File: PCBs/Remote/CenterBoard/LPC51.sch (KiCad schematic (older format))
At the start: 23 parts, among them J201 DX07S016JA1R1500, U201 LPC51U68JBD64

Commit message: Bezig met LEDS
Signed-off-by: Eldalote.Electronics <Eldalote.Electronics@gmail.com>
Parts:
- added C?: 100nF, Capacitor_SMD:C_0402_1005Metric, symbol Device:C_Small
- added U?: W25Q128JVS, Package_SO:SOIC-8_5.23x5.23mm_P1.27mm, symbol Memory_Flash:W25Q128JVS
- R201, R202: footprint Resistor_SMD:R_0805_2012Metric_Pad1.15x1.40mm_HandSolder -> Resistor_SMD:R_0603_1608Metric_Pad1.05x0.95mm_HandSolder; DigiKey P123897CT-ND -> P123790CT-ND; Mouser 667-ERA-6AHD330V -> 667-ERA-3AHD330V
- R203, R204, R205, R206: footprint Resistor_SMD:R_0805_2012Metric_Pad1.15x1.40mm_HandSolder -> Resistor_SMD:R_0603_1608Metric_Pad1.05x0.95mm_HandSolder; DigiKey P3.3KBNCT-ND -> P123763CT-ND; LCSC C26010 -> C22978; Mouser 667-ERA-6AED332V -> 667-ERA-3AED332V
- S201, S202: Category Switches -> (none); DK_Datasheet_Link https://www.te.com/commerce/DocumentDelivery/DDEController?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 -> (none); DK_Detail_Page /product-detail/en/te-connectivity-alcoswitch-switches/1825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 -> (none); Description SWITCH TACTILE SPST-NO 0.05A 24V -> (none); Digi-Key_PN 450-1650-ND -> (none); DigiKey (none) -> 450-1650-ND; Family Tactile Switches -> (none); MPN 1825910-6 -> (none); Manufacturer TE Connectivity ALCOSWITCH Switches -> (none); Mouser (none) -> 506-FSM4JH; Status Active -> (none)
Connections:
- net +3V3: now also C?.1, U?.8 (VCC)
- net GND: now also C?.2, U?.4 (GND)

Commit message: Continued work with the center board
Signed-off-by: Eldalote.Electronics <Eldalote.Electronics@gmail.com>
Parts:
- U201: DigiKey (none) -> 568-13909-ND; Mouser (none) -> 771-LPC51U68JBD64QL
- U202: renamed from U?; LCSC (none) -> C97521
- gave numbers to parts that had none: 1
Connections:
- net Flash_SPI_MISO: now reaches U202.2 (DO(IO1))
- net Flash_SPI_MOSI: now reaches U202.5 (DI(IO0))
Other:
- note added: "USB Connector"
- note added: "User Flash"
- moved on the sheet: C201, C202, C203, C204, C205, C206, C207, C208, C209, C210, C211, C212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

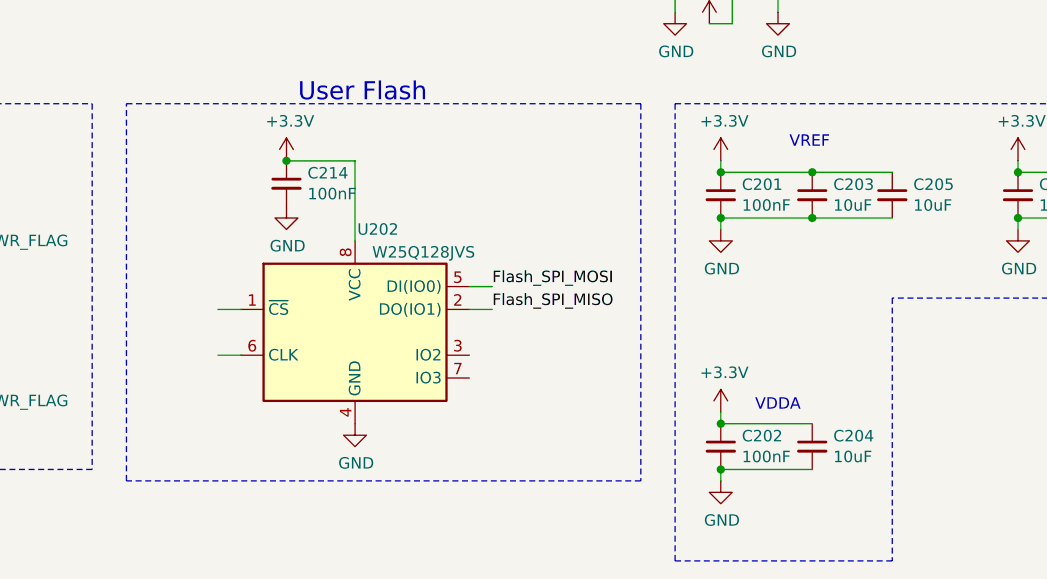
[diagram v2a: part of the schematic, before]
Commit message: Note: Schmitt trigger for joystick Buttons TODO
Signed-off-by: Eldalote.Electronics <Eldalote.Electronics@gmail.com>
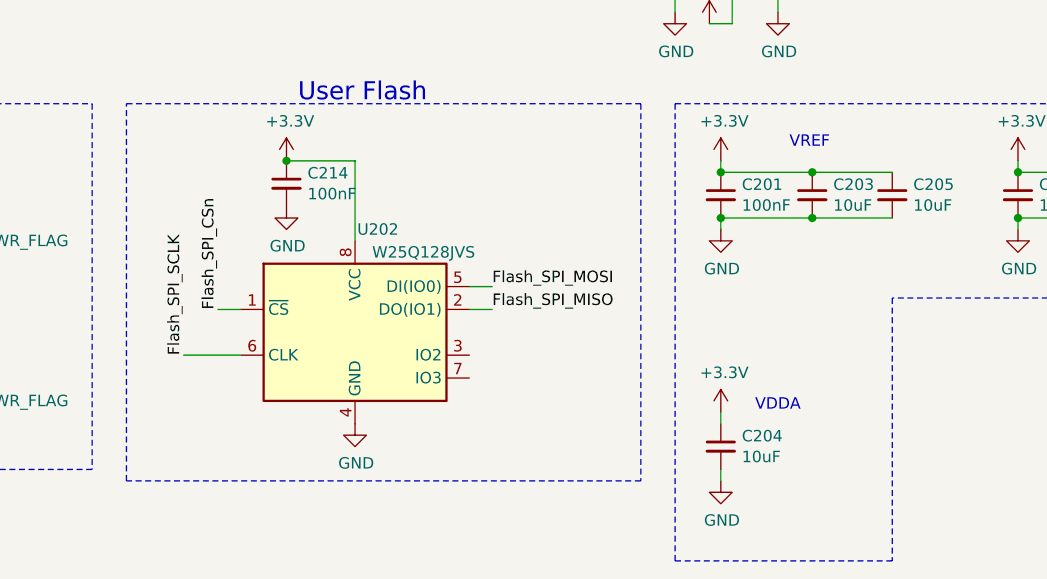
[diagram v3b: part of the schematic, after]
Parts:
- removed C202: 100nF, Capacitor_SMD:C_0805_2012Metric_Pad1.15x1.40mm_HandSolder, symbol Device:C_Small
- C201, C206, C208, C210, C212: footprint Capacitor_SMD:C_0805_2012Metric_Pad1.15x1.40mm_HandSolder -> Capacitor_SMD:C_0402_1005Metric; DigiKey 1276-1099-1-ND -> (none); LCSC C49678 -> C1525; Mouser 187-CL21B104KACNNNC -> (none)
- C203, C204, C205: footprint Capacitor_SMD:C_0805_2012Metric_Pad1.15x1.40mm_HandSolder -> Capacitor_SMD:C_0402_1005Metric; DigiKey 1276-2891-1-ND -> (none); LCSC C15850 -> C15525; Mouser 187-CL21A106KAYNNNE -> (none)
- C207, C209, C211, C213: footprint Capacitor_SMD:C_0805_2012Metric_Pad1.15x1.40mm_HandSolder -> Capacitor_SMD:C_0402_1005Metric; DigiKey 1276-1015-1-ND -> 1276-1028-1-ND; LCSC C1710 -> C15195; Mouser 187-CL21B103KBANNNC -> 187-CL05B103KB5NNNC
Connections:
- net Flash_SPI_CSn: now reaches U202.1 (~CS)
- net Flash_SPI_SCLK: now reaches U202.6 (CLK)

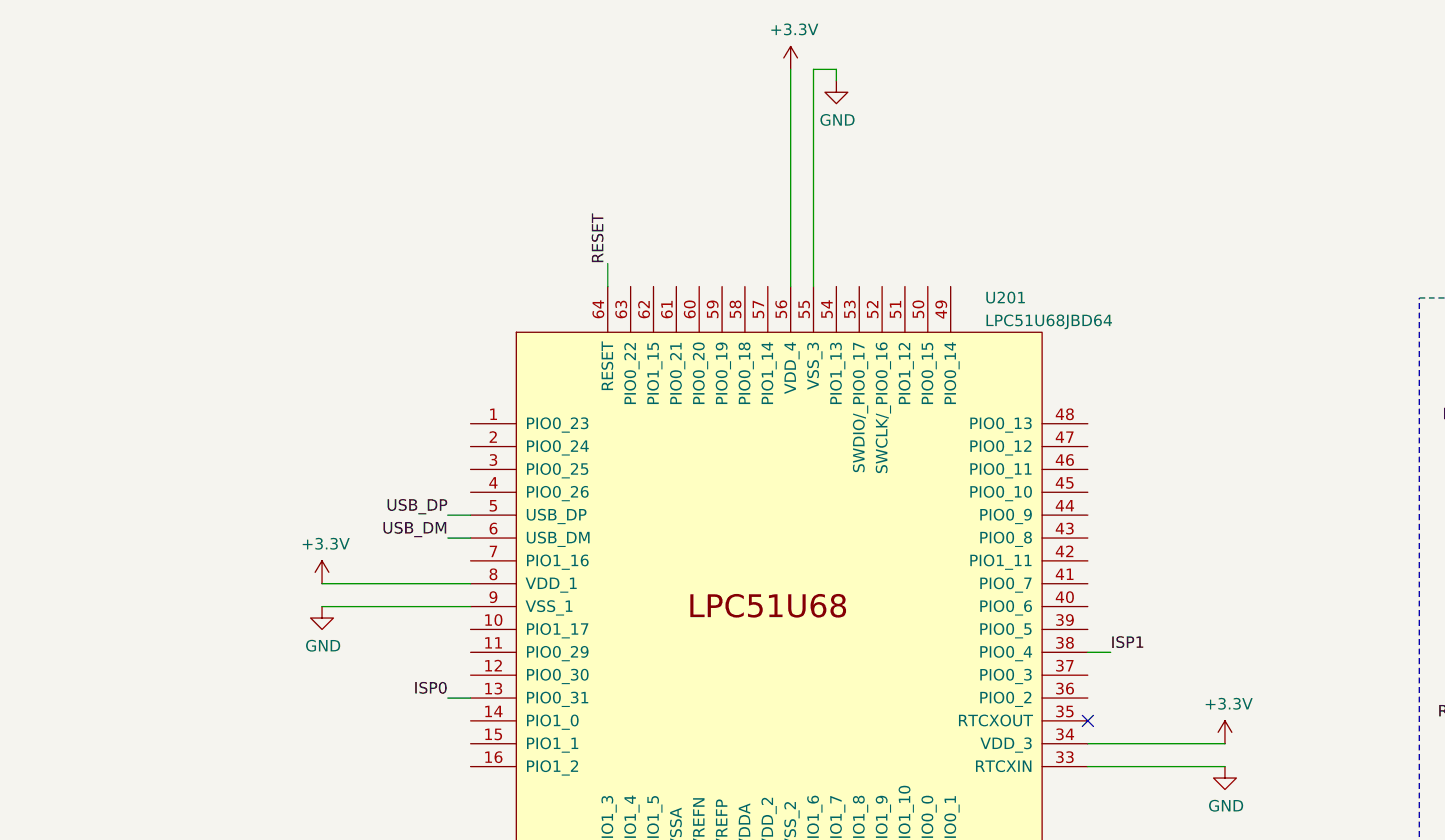
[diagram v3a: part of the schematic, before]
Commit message: Made the keyboard PCB. With LPC software started pin assignment on the LPC
Signed-off-by: Eldalote.Electronics <Eldalote.Electronics@gmail.com>
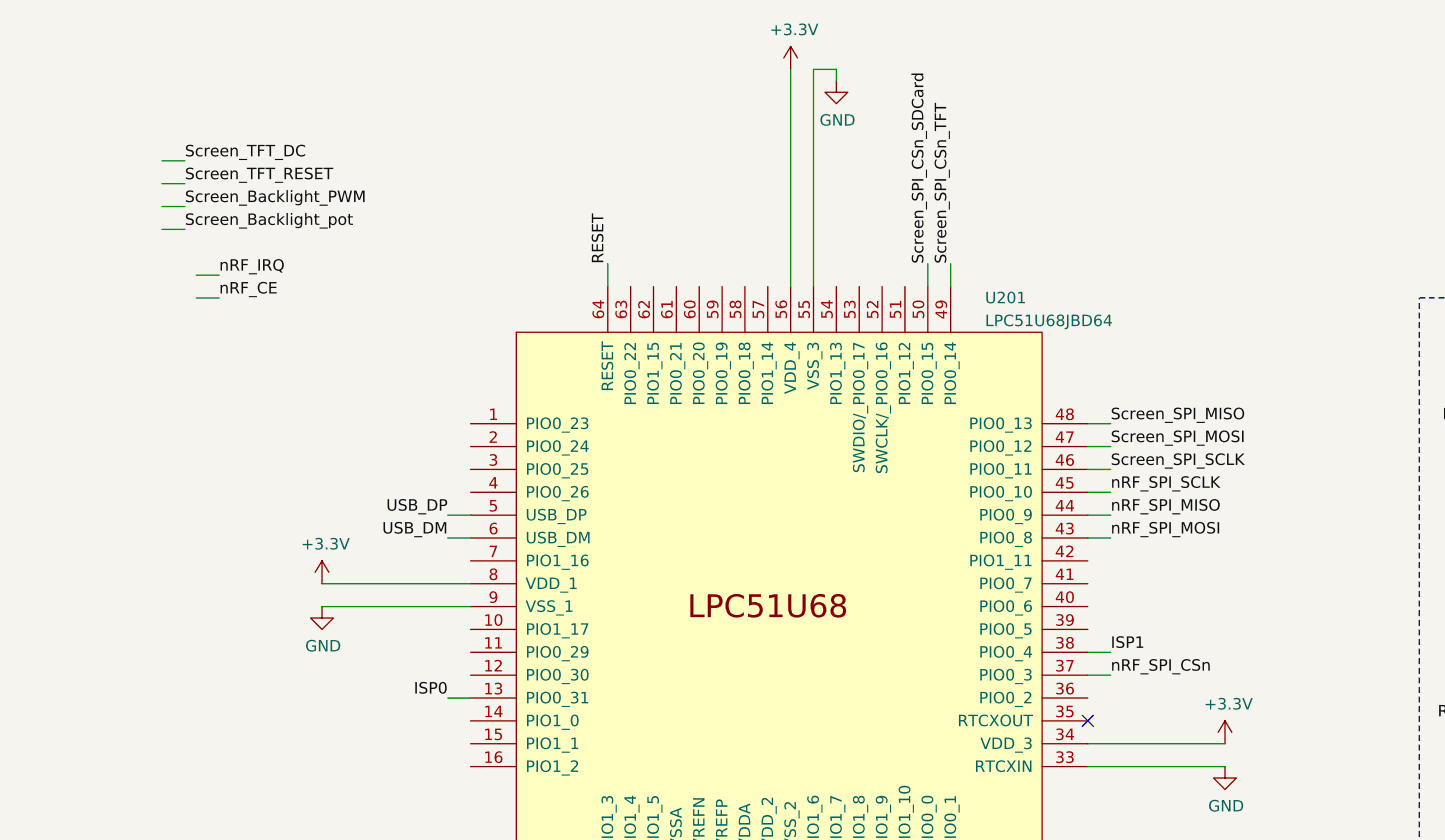
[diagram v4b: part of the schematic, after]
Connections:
- wire segments 117 -> 132
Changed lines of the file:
@@
 $Descr A4 11693 8268
 encoding utf-8
-Sheet 2 6
+Sheet 2 7
 Title ""
 Date ""
@@
 Text Label 3800 6650 1    50   ~ 0
 Flash_SPI_SCLK
+Wire Wire Line
+	7700 2800 7800 2800
+Wire Wire Line
+	7700 2700 7800 2700
+Wire Wire Line
+	7700 2600 7800 2600
+Wire Wire Line
+	7700 3400 7800 3400
+Wire Wire Line
+	3800 1750 3900 1750
+Wire Wire Line
+	3800 1650 3900 1650
+Text Label 7800 2600 0    50   ~ 0
+nRF_SPI_SCLK
+Text Label 7800 2700 0    50   ~ 0
+nRF_SPI_MISO
+Text Label 7800 2800 0    50   ~ 0
+nRF_SPI_MOSI
+Text Label 7800 3400 0    50   ~ 0
+nRF_SPI_CSn
+Text Label 3900 1650 0    50   ~ 0
+nRF_IRQ
+Text Label 3900 1750 0    50   ~ 0
+nRF_CE
+Wire Wire Line
+	3750 1450 3650 1450
+Text Label 3750 1450 0    50   ~ 0
+Screen_Backlight_pot
+Wire Wire Line
+	7700 2500 7800 2500
+Wire Wire Line
+	7700 2300 7800 2300
+Wire Wire Line
+	7700 2400 7800 2400
+Wire Wire Line
+	7100 1700 7100 1600
+Wire Wire Line
+	3650 1250 3750 1250
+Wire Wire Line
+	3650 1150 3750 1150
+Wire Wire Line
+	7000 1700 7000 1600
+Wire Wire Line
+	3650 1350 3750 1350
+Text Label 7800 2500 0    50   ~ 0
+Screen_SPI_SCLK
+Text Label 7800 2300 0    50   ~ 0
+Screen_SPI_MISO
+Text Label 7800 2400 0    50   ~ 0
+Screen_SPI_MOSI
+Text Label 7100 1600 1    50   ~ 0
+Screen_SPI_CSn_TFT
+Text Label 3750 1250 0    50   ~ 0
+Screen_TFT_RESET
+Text Label 3750 1150 0    50   ~ 0
+Screen_TFT_DC
+Text Label 7000 1600 1    50   ~ 0
+Screen_SPI_CSn_SDCard
+Text Label 3750 1350 0    50   ~ 0
+Screen_Backlight_PWM
 $EndSCHEMATC

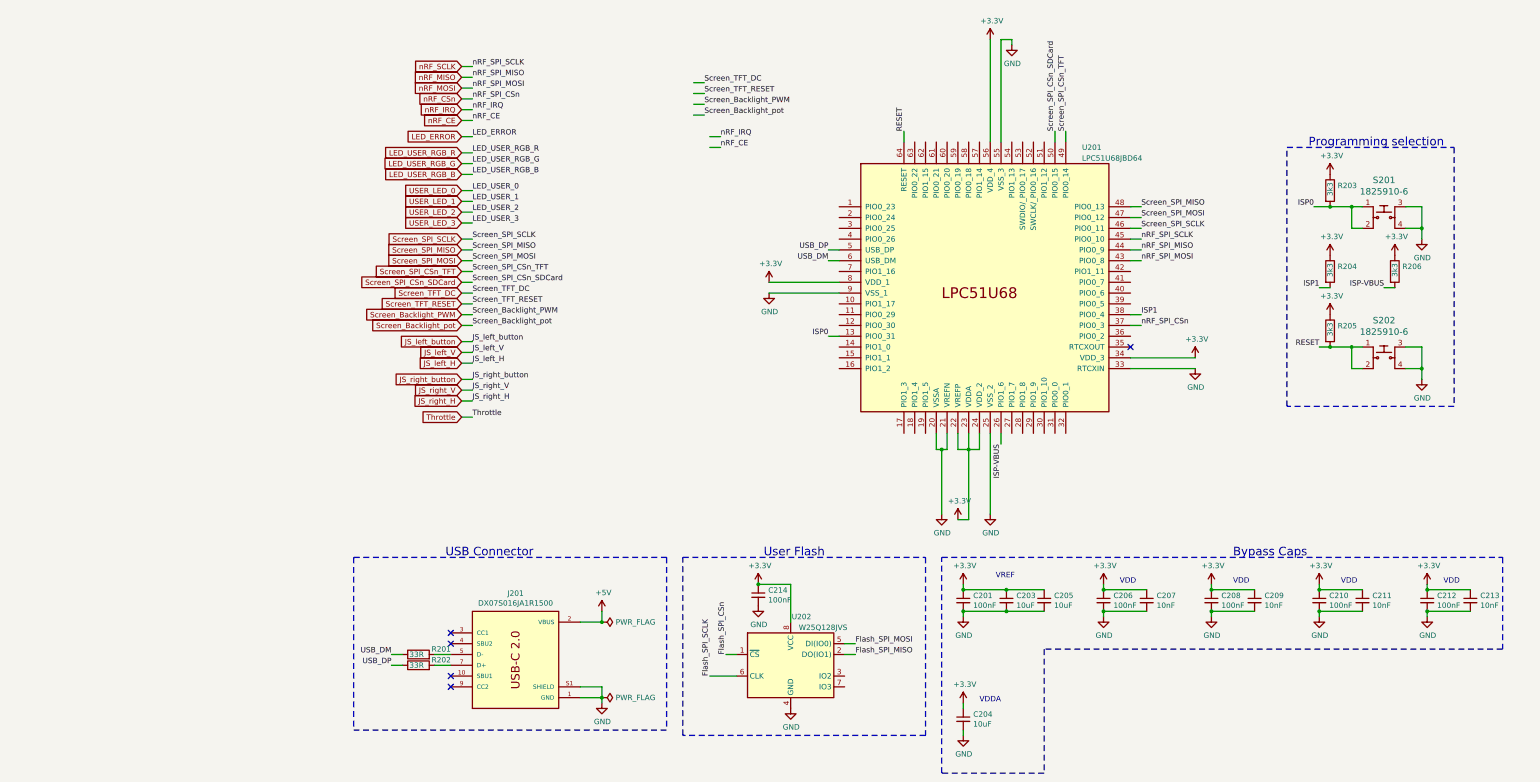
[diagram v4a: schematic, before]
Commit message: Screen POT->PWM and RGB LEDS reworked, making space on the CPU pins. Almost done
Signed-off-by: Eldalote.Electronics <Eldalote.Electronics@gmail.com>
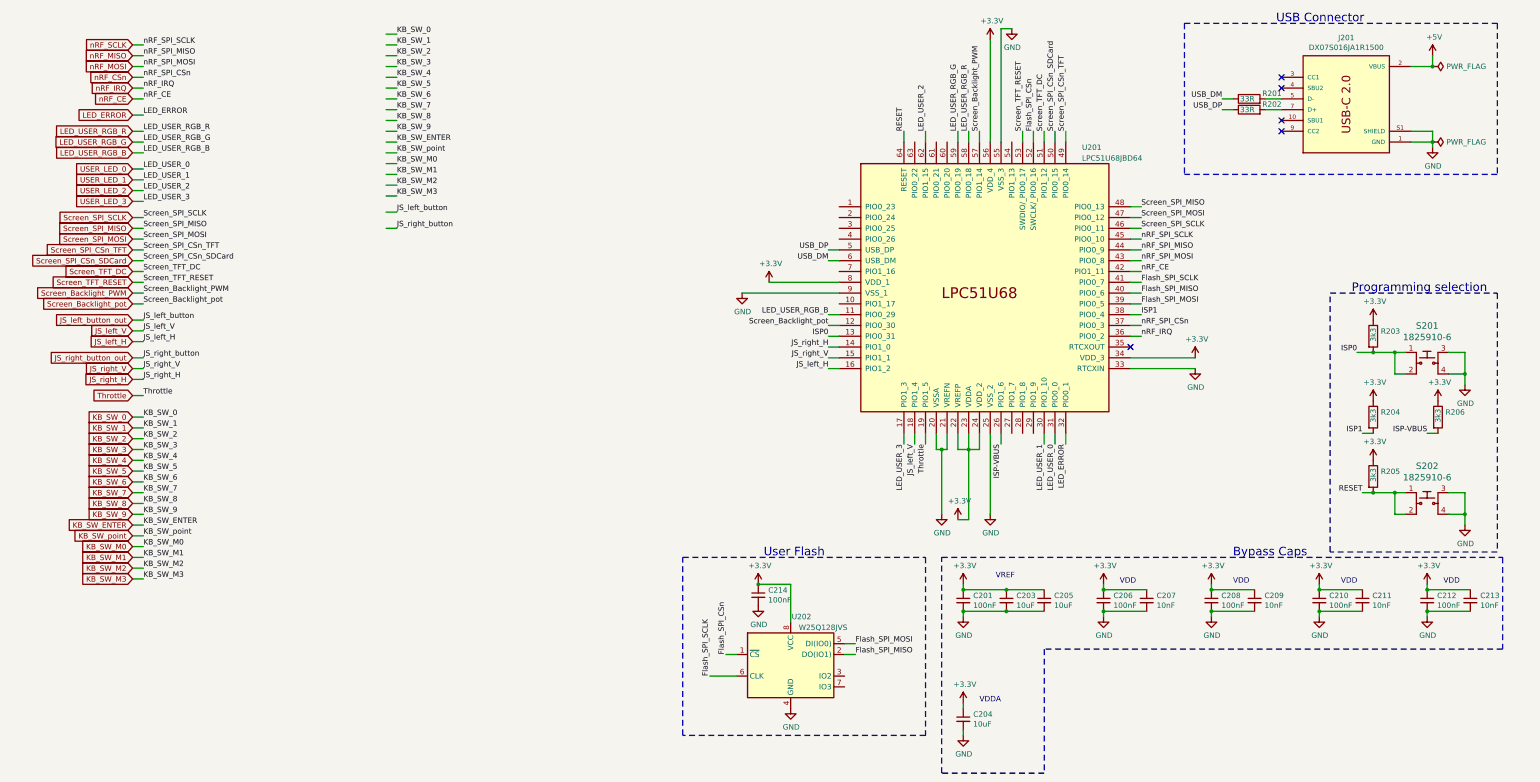
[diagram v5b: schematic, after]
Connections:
- net labels added: JS_left_button_out, JS_right_button_out, KB_SW_0, KB_SW_1, KB_SW_2, KB_SW_3, KB_SW_4, KB_SW_5, KB_SW_6, KB_SW_7, KB_SW_8, KB_SW_9, KB_SW_ENTER, KB_SW_M0, KB_SW_M1, KB_SW_M2, KB_SW_M3, KB_SW_point
- wire segments 132 -> 182
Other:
- moved on the sheet: J201, R201, R202, R203, R204, R205, R206, S201, S202
